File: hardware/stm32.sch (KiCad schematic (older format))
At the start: 29 parts, among them J6 PROG, Q1 PMBT3906,215, Q2 PMBT3906,215, Q3 PMBT3906,215, Q4 PMBT3906,215, Q5 PMBT3906,215, Q6 PMBT3906,215, Q7 PMBT3906,215, Q8 PMBT3906,215, U7 STM32F103C8Tx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

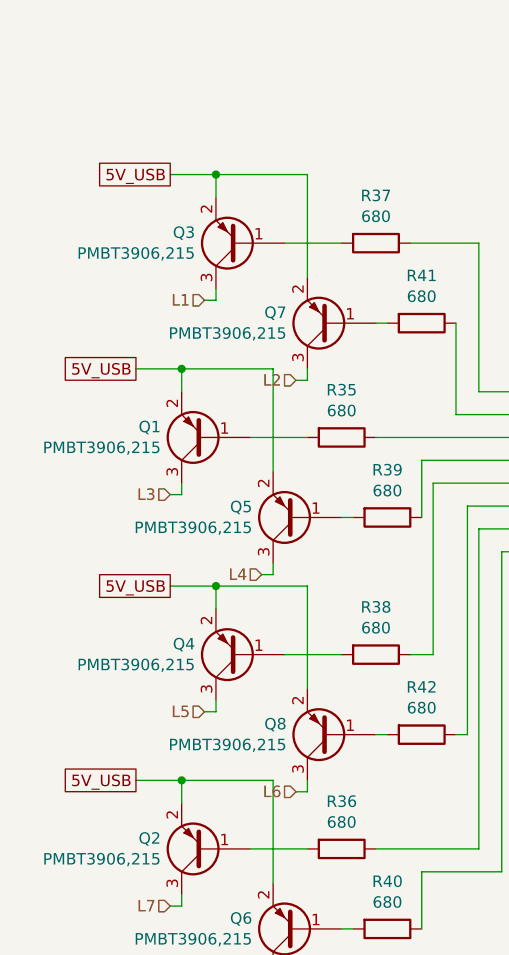
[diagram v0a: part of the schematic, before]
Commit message: Added battery circuit
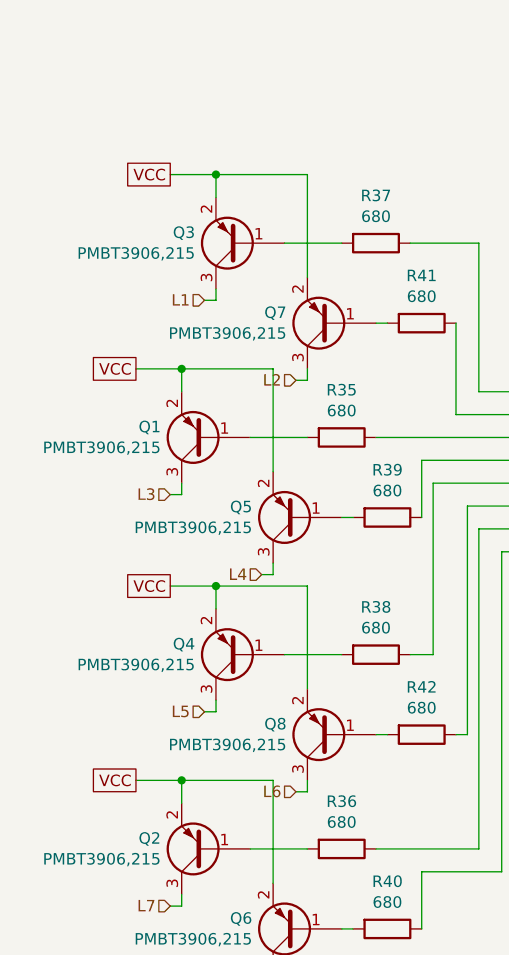
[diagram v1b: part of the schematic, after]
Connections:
- net 5V_USB renamed VCC
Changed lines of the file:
@@
 $Descr A4 11693 8268
 encoding utf-8
-Sheet 4 5
+Sheet 4 6
 Title ""
 Date ""
@@
 $EndComp
 Text GLabel 1150 3100 0    50   UnSpc ~ 0
-5V_USB
+VCC
 Wire Wire Line
 	1150 3100 1350 3100
@@
 	2500 3400 2500 4050
 Text GLabel 1000 3950 0    50   UnSpc ~ 0
-5V_USB
+VCC
 Wire Wire Line
 	1000 3950 1200 3950
@@
 	2250 4350 2250 4600
 Text GLabel 1150 4900 0    50   UnSpc ~ 0
-5V_USB
+VCC
 Wire Wire Line
 	1150 4900 1350 4900
@@
 	1650 5200 1900 5200
 Text GLabel 1000 5750 0    50   UnSpc ~ 0
-5V_USB
+VCC
 Wire Wire Line
 	1000 5750 1200 5750

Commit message: Wrover fp
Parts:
- TP2: footprint (none) -> TestPoint:TestPoint_Pad_D1.5mm
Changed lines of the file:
@@
 F 0 "TP2" H 3808 2468 50  0000 L CNN
 F 1 "Nrst" H 3808 2377 50  0000 L CNN
-F 2 "" H 3950 2350 50  0001 C CNN
+F 2 "TestPoint:TestPoint_Pad_D1.5mm" H 3950 2350 50  0001 C CNN
 F 3 "~" H 3950 2350 50  0001 C CNN
 	1    3750 2350

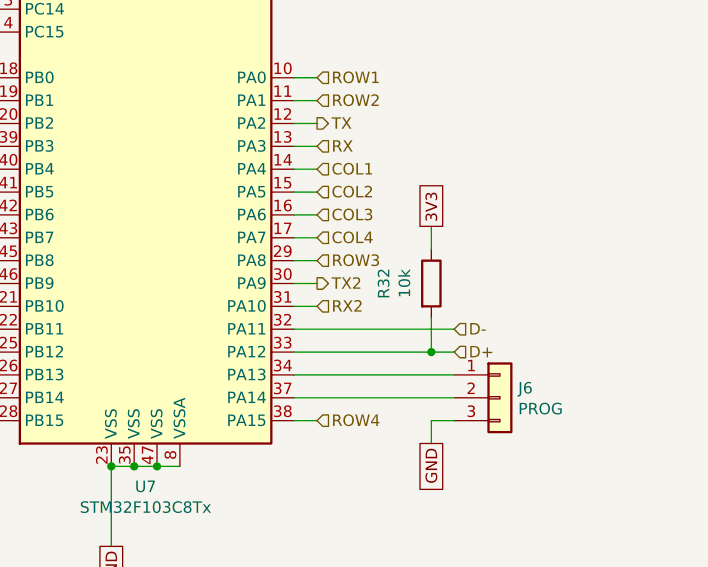
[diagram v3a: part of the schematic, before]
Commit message: Updated resistor to 1.5k according to stm datasheet
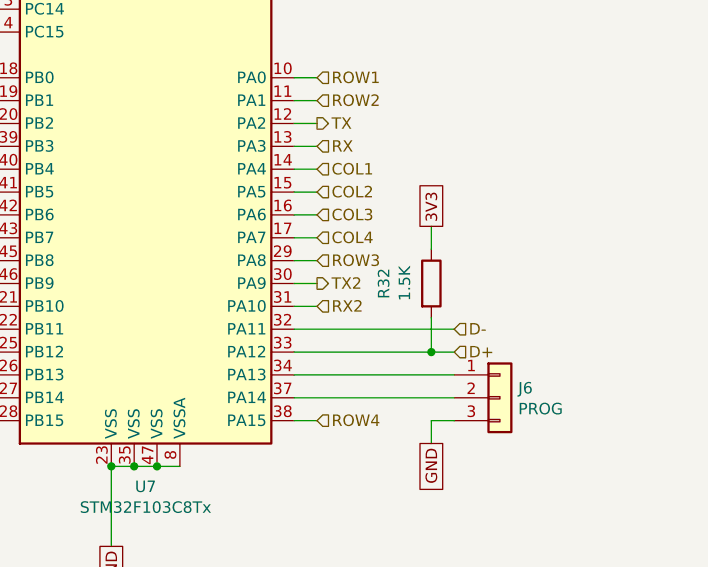
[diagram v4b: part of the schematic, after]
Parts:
- R32: value 10k -> 1.5K; LCSC C25804 -> (none)
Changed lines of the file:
@@
 EESchema Schematic File Version 4
-LIBS:cz-badge-hardware-cache
 EELAYER 30 0
 EELAYER END
 $Descr A4 11693 8268
 encoding utf-8
-Sheet 4 6
+Sheet 6 6
 Title ""
 Date ""
@@
 AR Path="/5E3BA64A/5E4109CF" Ref="R32"  Part="1"
 F 0 "R32" V 6193 4400 50  0000 C CNN
-F 1 "10k" V 6284 4400 50  0000 C CNN
+F 1 "1.5K" V 6284 4400 50  0000 C CNN
 F 2 "Resistor_SMD:R_0603_1608Metric" V 6330 4400 50  0001 C CNN
 F 3 "~" H 6400 4400 50  0001 C CNN
-F 4 "C25804" H 6400 4400 50  0001 C CNN "LCSC"
+F 4 "" H 6400 4400 50  0001 C CNN "LCSC"
 	1    6400 4400
 	1    0    0    -1

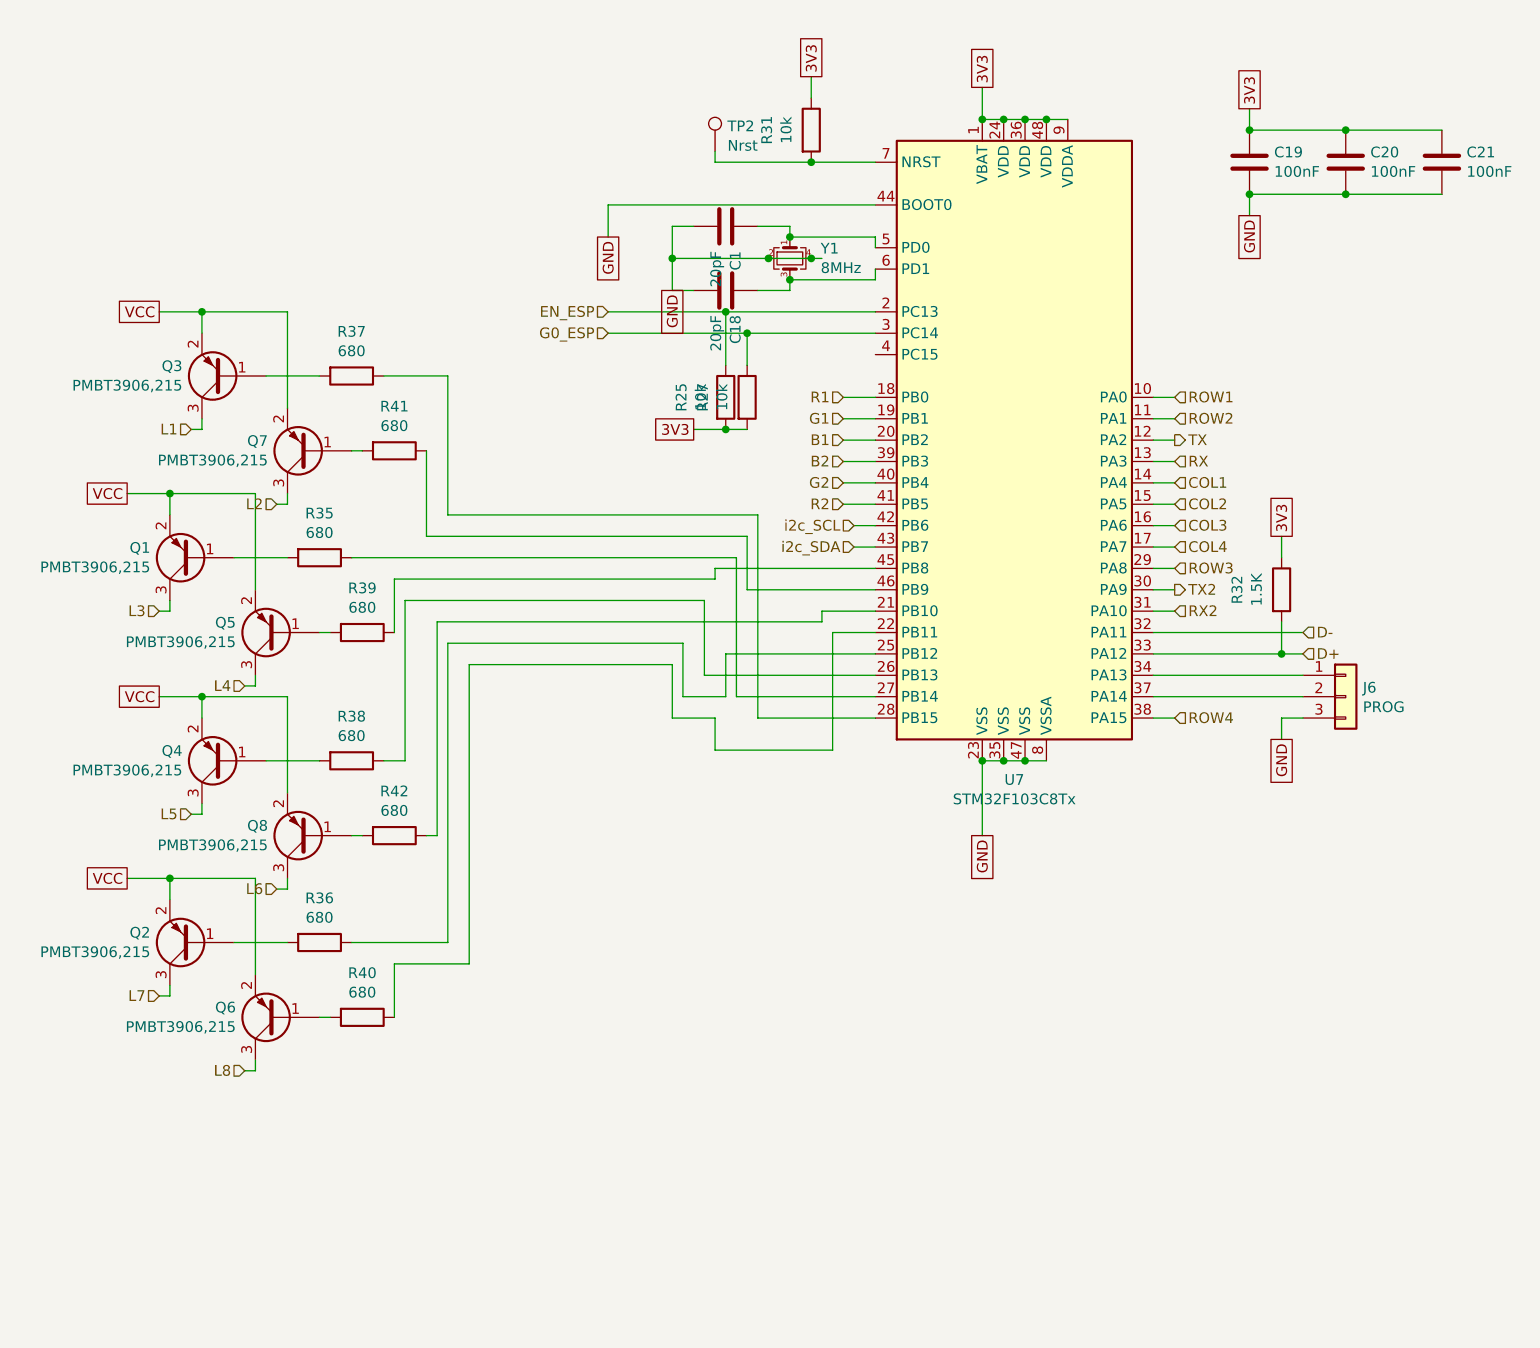
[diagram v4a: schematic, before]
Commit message: Added n-fets to LEDs
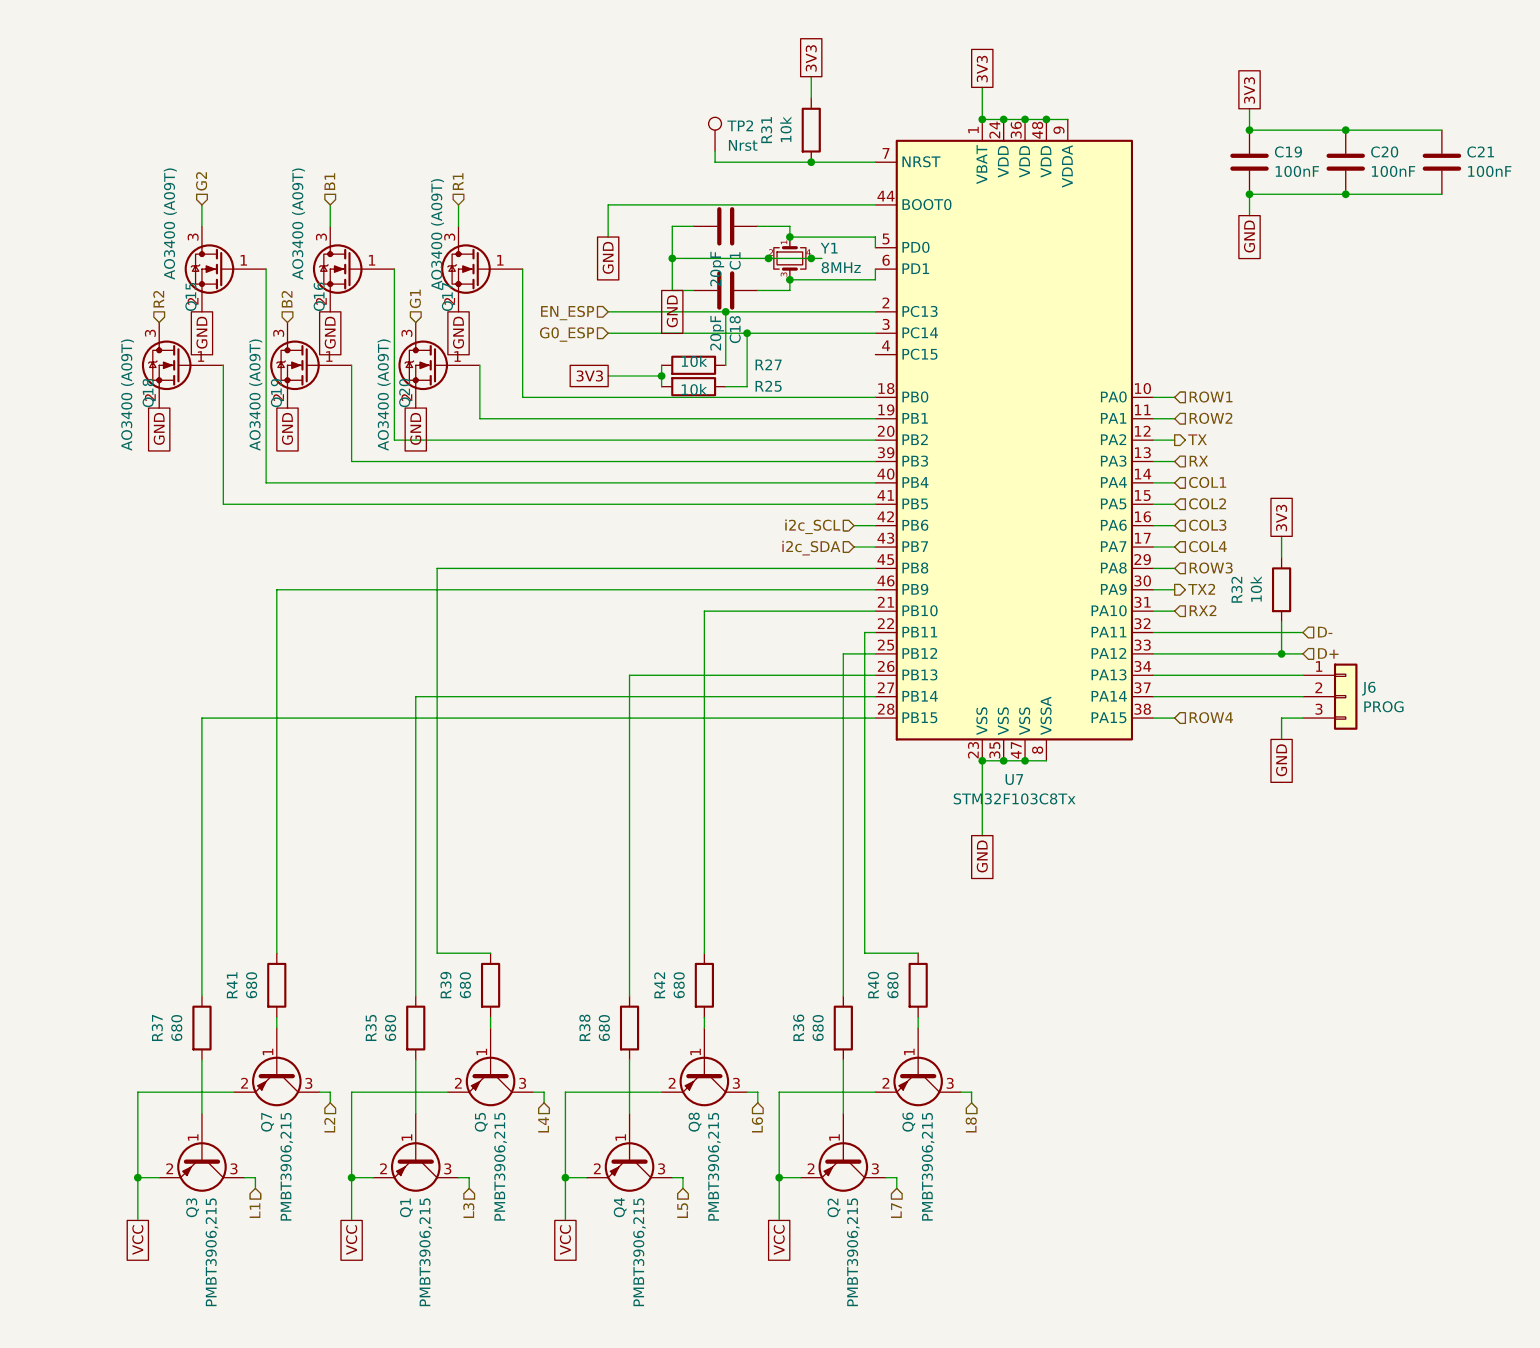
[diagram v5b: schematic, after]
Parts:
- added Q15, Q16, Q17, Q18, Q19, Q20: AO3400 (A09T), Package_TO_SOT_SMD:SOT-23, symbol Transistor_FET:DMN2050L
- R32: value 1.5K -> 10k; LCSC (none) -> C25804
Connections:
- net B1: now also Q16.3 (D); no longer U7.20 (PB2)
- net B2: now also Q19.3 (D); no longer U7.39 (PB3)
- net G1: now also Q20.3 (D); no longer U7.19 (PB1)
- net G2: now also Q15.3 (D); no longer U7.40 (PB4)
- net GND: now also Q15.2 (S), Q16.2 (S), Q17.2 (S), Q18.2 (S), Q19.2 (S), Q20.2 (S)
- net R1: now also Q17.3 (D); no longer U7.18 (PB0)
- net R2: now also Q18.3 (D); no longer U7.41 (PB5)
- new net: Q17.1 (G), U7.18 (PB0)
- new net: Q20.1 (G), U7.19 (PB1)
- new net: Q16.1 (G), U7.20 (PB2)
- new net: Q19.1 (G), U7.39 (PB3)
- new net: Q15.1 (G), U7.40 (PB4)
- new net: Q18.1 (G), U7.41 (PB5)
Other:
- moved on the sheet: Q1, Q2, Q3, Q4, Q5, Q6, Q7, Q8, R25, R27, R35, R36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

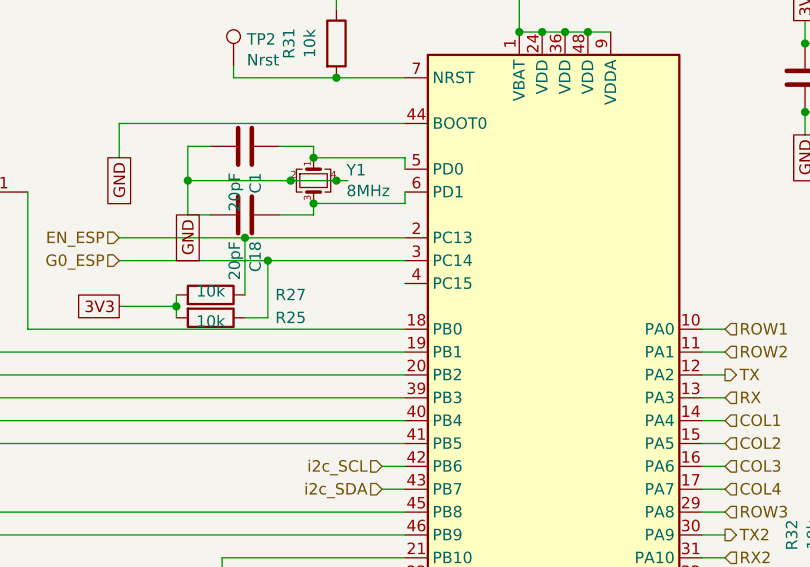
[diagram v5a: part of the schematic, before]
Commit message: Changed connectors to smd and added powerswitch
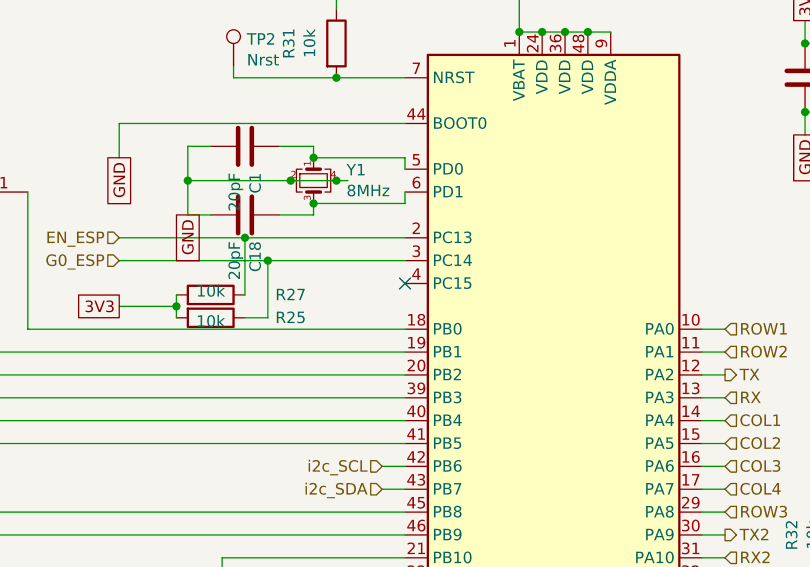
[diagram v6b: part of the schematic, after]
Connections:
- no-connect marks 0 -> 1
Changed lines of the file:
@@
 Text GLabel 1150 3550 3    50   UnSpc ~ 0
 GND
+NoConn ~ 4500 3300
 $EndSCHEMATC

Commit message: Production data rev4
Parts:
- Y1: LCSC C280087 -> C13738
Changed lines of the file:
@@
 F 2 "Crystal:Crystal_SMD_3225-4Pin_3.2x2.5mm" H 4100 2850 50  0001 C CNN
 F 3 "~" H 4100 2850 50  0001 C CNN
-F 4 "C280087" H 4100 2850 50  0001 C CNN "LCSC"
+F 4 "C13738" H 4100 2850 50  0001 C CNN "LCSC"
 	1    4100 2850
 	0    1    1    0

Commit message: Updated production files: - vias in 8-pin female header - fixed some text elements - added testpoint for FLASH
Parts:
- Y1: LCSC C13738 -> C280087
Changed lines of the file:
@@
 F 2 "Crystal:Crystal_SMD_3225-4Pin_3.2x2.5mm" H 4100 2850 50  0001 C CNN
 F 3 "~" H 4100 2850 50  0001 C CNN
-F 4 "C13738" H 4100 2850 50  0001 C CNN "LCSC"
+F 4 "C280087" H 4100 2850 50  0001 C CNN "LCSC"
 	1    4100 2850
 	0    1    1    0
